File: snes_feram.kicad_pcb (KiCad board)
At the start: 2 copper layers, 98.5 x 79.5 mm, 35 parts, among them CON1 SNES-EDGE, J1 Conn_01x23_Male, J2 Conn_01x23_Male, SW1 SW_DIP_x04, U1 4081, U2 4071, U3 27C322, U5 74LS245, U6 74LS245, U7 74LS139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

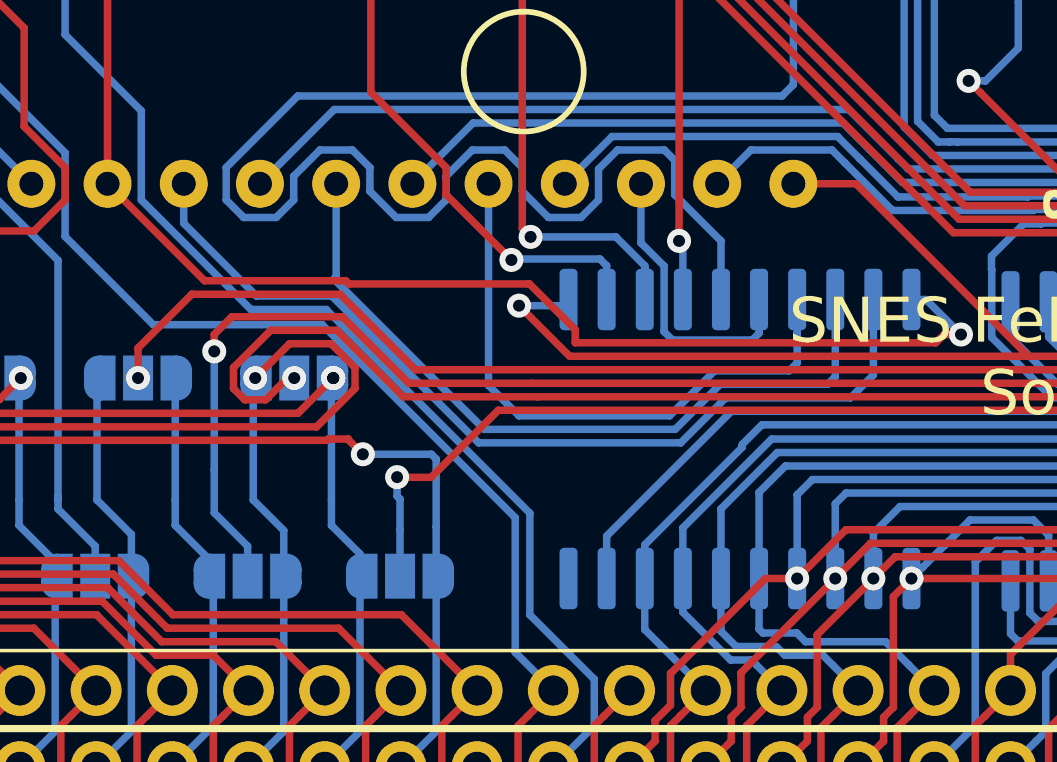
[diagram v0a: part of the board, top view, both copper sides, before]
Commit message: Corrected missing trace at pin 20 of U5, thanks to @DeLFuS
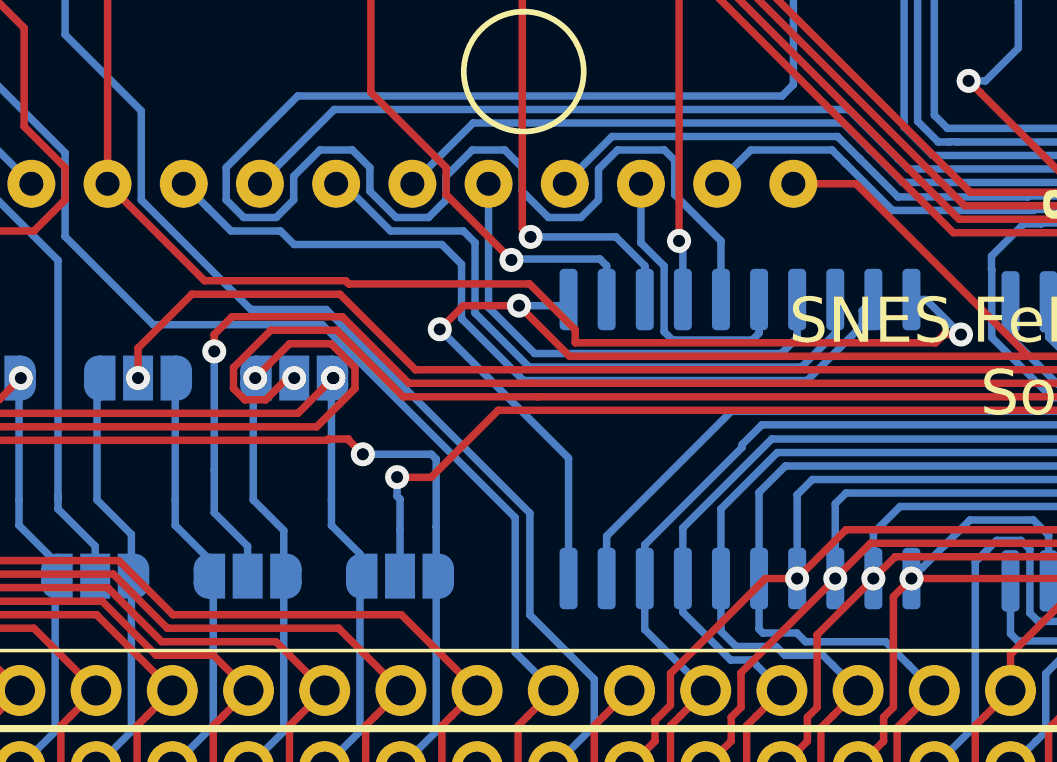
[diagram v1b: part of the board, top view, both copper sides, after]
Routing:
- net +5V: track 262.5 -> 275.5 mm, vias 10 -> 11
- net /D13: track 20.3 -> 16.5 mm
- net /D14: track 25.3 -> 22.1 mm
- net /D15: track 30.8 -> 28.2 mm
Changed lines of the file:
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@@
     (thickness 1.6)
     (drawings 48)
-    (tracks 2026)
+    (tracks 2032)
     (zones 0)
     (modules 35)
@@
       (drillshape 0)
       (scaleselection 1)
-      (outputdirectory ""))
+      (outputdirectory "Gerber/"))
   )
   (net 0 "")
@@
   (segment (start 143.41895 82.07795) (end 158.71405 82.07795) (width 0.25) (layer F.Cu) (net 2))
   (segment (start 158.71405 82.07795) (end 167.35005 82.07795) (width 0.25) (layer F.Cu) (net 2))
+  (via (at 139.0904 81.1784) (size 0.8) (drill 0.4) (layers F.Cu B.Cu) (net 2))
+  (segment (start 143.383 89.486) (end 143.383 85.471) (width 0.25) (layer B.Cu) (net 2))
+  (segment (start 143.383 85.471) (end 139.0904 81.1784) (width 0.25) (layer B.Cu) (net 2))
+  (segment (start 139.8778 80.391) (end 141.732 80.391) (width 0.25) (layer F.Cu) (net 2))
+  (segment (start 139.0904 81.1784) (end 139.8778 80.391) (width 0.25) (layer F.Cu) (net 2))
   (via (at 105.791 51.971129) (size 0.8) (drill 0.4) (layers F.Cu B.Cu) (net 3))
   (segment (start 105.791 51.405444) (end 105.791 45.388) (width 0.25) (layer F.Cu) (net 3) (status 20))
@@
   (segment (start 143.256 76.327) (end 144.831011 74.751989) (width 0.25) (layer B.Cu) (net 73))
   (segment (start 154.3644 76.76599) (end 153.099205 75.500795) (width 0.25) (layer B.Cu) (net 73))
-  (segment (start 151.003 80.186) (end 151.003 81.311) (width 0.25) (layer B.Cu) (net 74))
-  (segment (start 151.003 81.311) (end 151.003 82.296) (width 0.25) (layer B.Cu) (net 74))
-  (segment (start 150.73597 82.56303) (end 148.250855 82.563031) (width 0.25) (layer B.Cu) (net 74))
-  (segment (start 151.003 82.296) (end 150.73597 82.56303) (width 0.25) (layer B.Cu) (net 74))
-  (segment (start 148.250855 82.563031) (end 146.750906 84.06298) (width 0.25) (layer B.Cu) (net 74))
-  (segment (start 140.716 76.327) (end 140.716 83.04698) (width 0.25) (layer B.Cu) (net 74))
-  (segment (start 141.732 84.06298) (end 146.750906 84.06298) (width 0.25) (layer B.Cu) (net 74))
-  (segment (start 140.716 83.04698) (end 141.732 84.06298) (width 0.25) (layer B.Cu) (net 74))
+  (segment (start 151.003 81.4578) (end 151.003 80.186) (width 0.25) (layer B.Cu) (net 74))
+  (segment (start 150.47478 81.98602) (end 151.003 81.4578) (width 0.25) (layer B.Cu) (net 74))
+  (segment (start 142.254018 81.98602) (end 150.47478 81.98602) (width 0.25) (layer B.Cu) (net 74))
+  (segment (start 140.716 80.448002) (end 142.254018 81.98602) (width 0.25) (layer B.Cu) (net 74))
+  (segment (start 140.716 76.327) (end 140.716 80.448002) (width 0.25) (layer B.Cu) (net 74))
   (segment (start 154.518789 76.283969) (end 153.429215 75.194395) (width 0.25) (layer B.Cu) (net 75))
   (segment (start 169.010791 76.283969) (end 154.518789 76.283969) (width 0.25) (layer B.Cu) (net 75))
@@
   (segment (start 140.201021 74.301979) (end 152.536799 74.301979) (width 0.25) (layer B.Cu) (net 75))
   (segment (start 138.176 76.327) (end 140.201021 74.301979) (width 0.25) (layer B.Cu) (net 75))
-  (segment (start 152.273 80.186) (end 152.273 82.759039) (width 0.25) (layer B.Cu) (net 76))
-  (segment (start 152.018999 83.01304) (end 148.437256 83.01304) (width 0.25) (layer B.Cu) (net 76))
-  (segment (start 152.273 82.759039) (end 152.018999 83.01304) (width 0.25) (layer B.Cu) (net 76))
-  (segment (start 148.437256 83.01304) (end 146.937306 84.51299) (width 0.25) (layer B.Cu) (net 76))
-  (segment (start 140.570558 84.51299) (end 135.559568 79.502) (width 0.25) (layer B.Cu) (net 76))
-  (segment (start 146.937306 84.51299) (end 140.570558 84.51299) (width 0.25) (layer B.Cu) (net 76))
-  (segment (start 135.636 79.425568) (end 135.636 76.327) (width 0.25) (layer B.Cu) (net 76))
-  (segment (start 135.559568 79.502) (end 135.636 79.425568) (width 0.25) (layer B.Cu) (net 76))
+  (segment (start 135.874588 76.327) (end 137.449599 77.902011) (width 0.25) (layer B.Cu) (net 76))
+  (segment (start 135.636 76.327) (end 135.874588 76.327) (width 0.25) (layer B.Cu) (net 76))
+  (segment (start 139.878011 77.902011) (end 140.26599 78.28999) (width 0.25) (layer B.Cu) (net 76))
+  (segment (start 137.449599 77.902011) (end 139.878011 77.902011) (width 0.25) (layer B.Cu) (net 76))
+  (segment (start 140.265991 80.634403) (end 142.067618 82.43603) (width 0.25) (layer B.Cu) (net 76))
+  (segment (start 140.26599 78.28999) (end 140.265991 80.634403) (width 0.25) (layer B.Cu) (net 76))
+  (segment (start 152.273 81.311) (end 152.273 80.186) (width 0.25) (layer B.Cu) (net 76))
+  (segment (start 151.14797 82.43603) (end 152.273 81.311) (width 0.25) (layer B.Cu) (net 76))
+  (segment (start 142.067618 82.43603) (end 151.14797 82.43603) (width 0.25) (layer B.Cu) (net 76))
   (segment (start 169.197191 75.833959) (end 154.705189 75.833959) (width 0.25) (layer B.Cu) (net 77))
   (segment (start 171.520037 78.156805) (end 169.197191 75.833959) (width 0.25) (layer B.Cu) (net 77))
@@
   (segment (start 133.096 76.327) (end 135.571031 73.851969) (width 0.25) (layer B.Cu) (net 77))
   (segment (start 154.705189 75.833959) (end 154.370615 75.499385) (width 0.25) (layer B.Cu) (net 77))
-  (segment (start 153.543 80.186) (end 153.543 82.701048) (width 0.25) (layer B.Cu) (net 78))
-  (segment (start 152.781 83.463048) (end 148.623657 83.463049) (width 0.25) (layer B.Cu) (net 78))
-  (segment (start 153.543 82.701048) (end 152.781 83.463048) (width 0.25) (layer B.Cu) (net 78))
-  (segment (start 147.123706 84.963) (end 140.384158 84.963) (width 0.25) (layer B.Cu) (net 78))
-  (segment (start 148.623657 83.463049) (end 147.123706 84.963) (width 0.25) (layer B.Cu) (net 78))
-  (segment (start 140.384158 84.963) (end 135.489148 80.06799) (width 0.25) (layer B.Cu) (net 78))
-  (segment (start 135.489148 80.06799) (end 132.9784 80.06799) (width 0.25) (layer B.Cu) (net 78))
-  (segment (start 130.556 77.64559) (end 130.556 76.327) (width 0.25) (layer B.Cu) (net 78))
-  (segment (start 132.9784 80.06799) (end 130.556 77.64559) (width 0.25) (layer B.Cu) (net 78))
+  (segment (start 131.355999 77.126999) (end 130.556 76.327) (width 0.25) (layer B.Cu) (net 78))
+  (segment (start 132.131011 77.902011) (end 131.355999 77.126999) (width 0.25) (layer B.Cu) (net 78))
+  (segment (start 133.782011 77.902011) (end 132.131011 77.902011) (width 0.25) (layer B.Cu) (net 78))
+  (segment (start 134.232021 78.352021) (end 133.782011 77.902011) (width 0.25) (layer B.Cu) (net 78))
+  (segment (start 139.159621 78.352021) (end 134.232021 78.352021) (width 0.25) (layer B.Cu) (net 78))
+  (segment (start 153.17229 80.55671) (end 153.17229 81.04812) (width 0.25) (layer B.Cu) (net 78))
+  (segment (start 153.17229 81.04812) (end 151.334371 82.886039) (width 0.25) (layer B.Cu) (net 78))
+  (segment (start 153.543 80.186) (end 153.17229 80.55671) (width 0.25) (layer B.Cu) (net 78))
+  (segment (start 151.334371 82.886039) (end 141.881217 82.886039) (width 0.25) (layer B.Cu) (net 78))
+  (segment (start 141.881217 82.886039) (end 139.815982 80.820802) (width 0.25) (layer B.Cu) (net 78))
+  (segment (start 139.815982 79.008382) (end 139.159621 78.352021) (width 0.25) (layer B.Cu) (net 78))
+  (segment (start 139.815982 80.820802) (end 139.815982 79.008382) (width 0.25) (layer B.Cu) (net 78))
   (via (at 165.735 78.486) (size 0.8) (drill 0.4) (layers F.Cu B.Cu) (net 79))
   (segment (start 167.005 79.756) (end 165.735 78.486) (width 0.25) (layer B.Cu) (net 79))

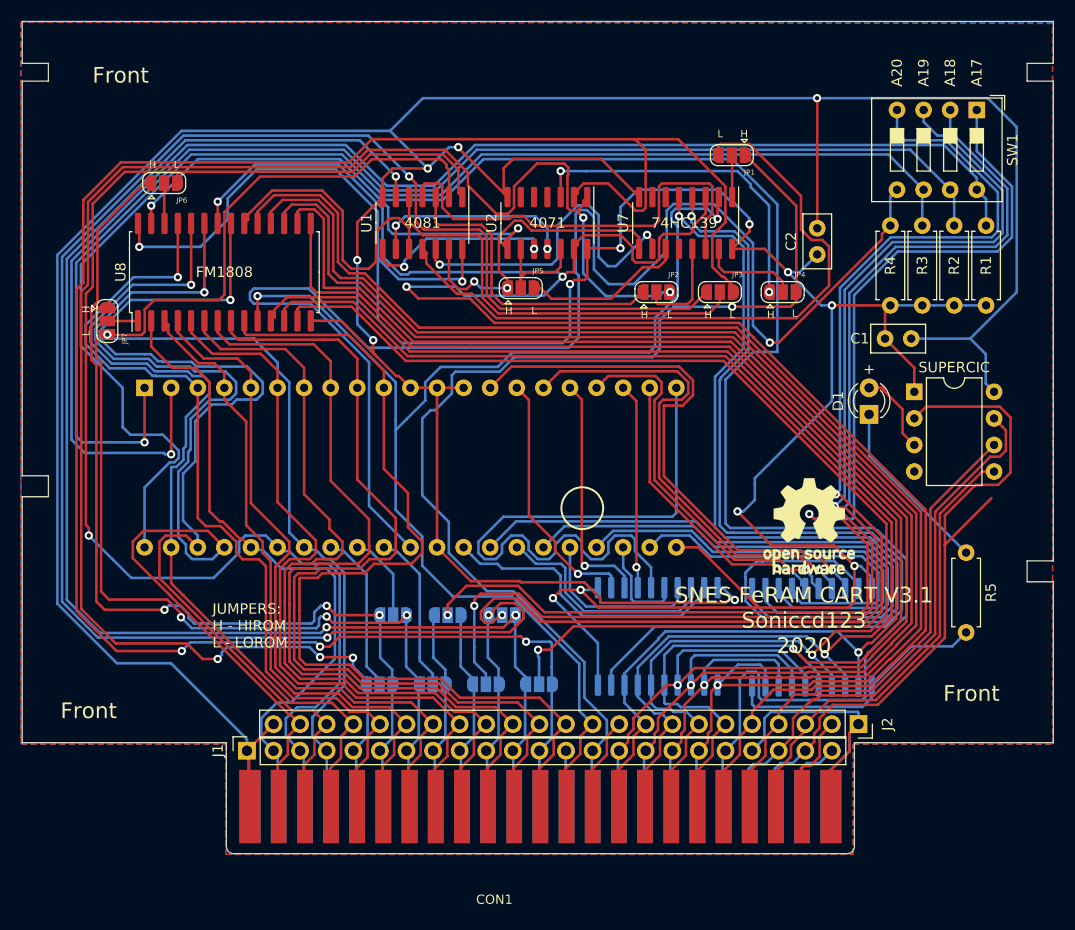
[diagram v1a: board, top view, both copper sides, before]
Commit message: -Upgrade to kicad6 -Fixed ERC errors -Edited soic footprints to indicate pin1 with a circle -Added Slash to Low asserted signals -Fixed byte swapping
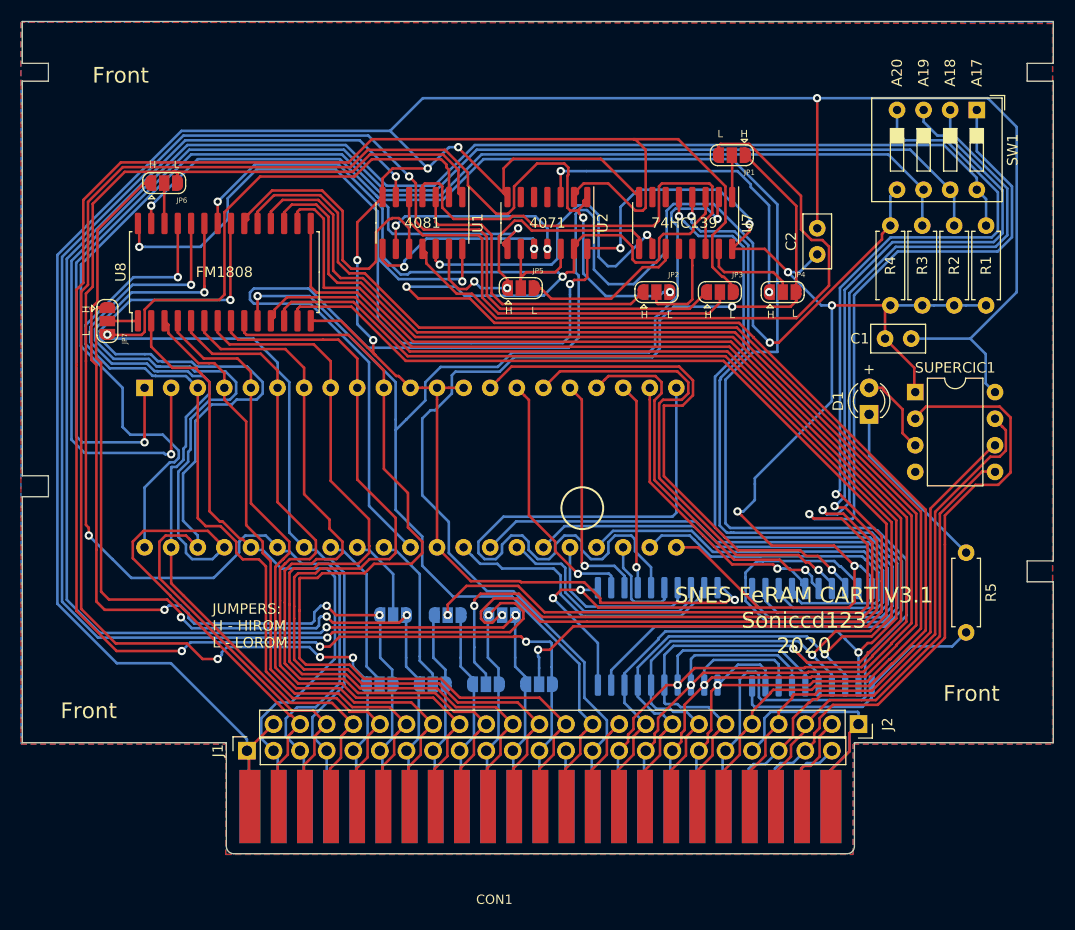
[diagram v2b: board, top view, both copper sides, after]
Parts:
- removed G***: LOGO, OPEN:open_hardware
- removed SUPERCIC: PIC12F629-IMC, Package_DIP:DIP-8_W7.62mm
- added SUPERCIC1: PIC12F629-IMC, Package_DIP:DIP-8_W7.62mm, F.Cu at (173.7, 61.5)
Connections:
- J1 pad 14: /CART -> //CART
- J1 pad 19: /WR -> //WR
- J2 pad 10: /IRQ -> //IRQ
- J2 pad 2: /RESET -> //RESET
- J2 pad 5: /RD -> //RD
- JP1 pad 1: /CART -> //CART
- JP4 pad 3: /CART -> //CART
- U2 pad 13: /RD -> //RD
- U2 pad 8: /WR -> //WR
- U7 pad 12: (no net) -> unconnected-(U7-Pad12)
- U7 pad 3: /RD -> //RD
- U7 pad 4: /BYTE_1 -> /BYTE_0
- U7 pad 5: /BYTE_0 -> /BYTE_1
- U7 pad 6: (no net) -> unconnected-(U7-Pad6)
- U7 pad 7: (no net) -> unconnected-(U7-Pad7)
- U8 pad 22: /RD -> //RD
- U8 pad 27: /WR -> //WR
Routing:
- net /RD: track 183.6 -> 0.00 mm, vias 3 -> 0
- net //WR: track 0.00 -> 182.7 mm, vias 0 -> 2
- net /WR: track 182.7 -> 0.00 mm, vias 2 -> 0
- net //RD: track 0.00 -> 180.1 mm, vias 0 -> 3
- net //CART: track 0.00 -> 105.6 mm, vias 0 -> 1
- net /CART: track 105.6 -> 0.00 mm, vias 1 -> 0
- net /IRQ: track 9.09 -> 0.00 mm
- net /CIC_CLK: track 67.1 -> 60.8 mm
- net //IRQ: track 0.00 -> 5.44 mm
- net /CIC_OUT: track 48.6 -> 45.1 mm
- net /BYTE_1: track 91.7 -> 90.5 mm
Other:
- net class Default removed

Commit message: -Fixed footprint library missing -Updated soic footprints -Updated version number
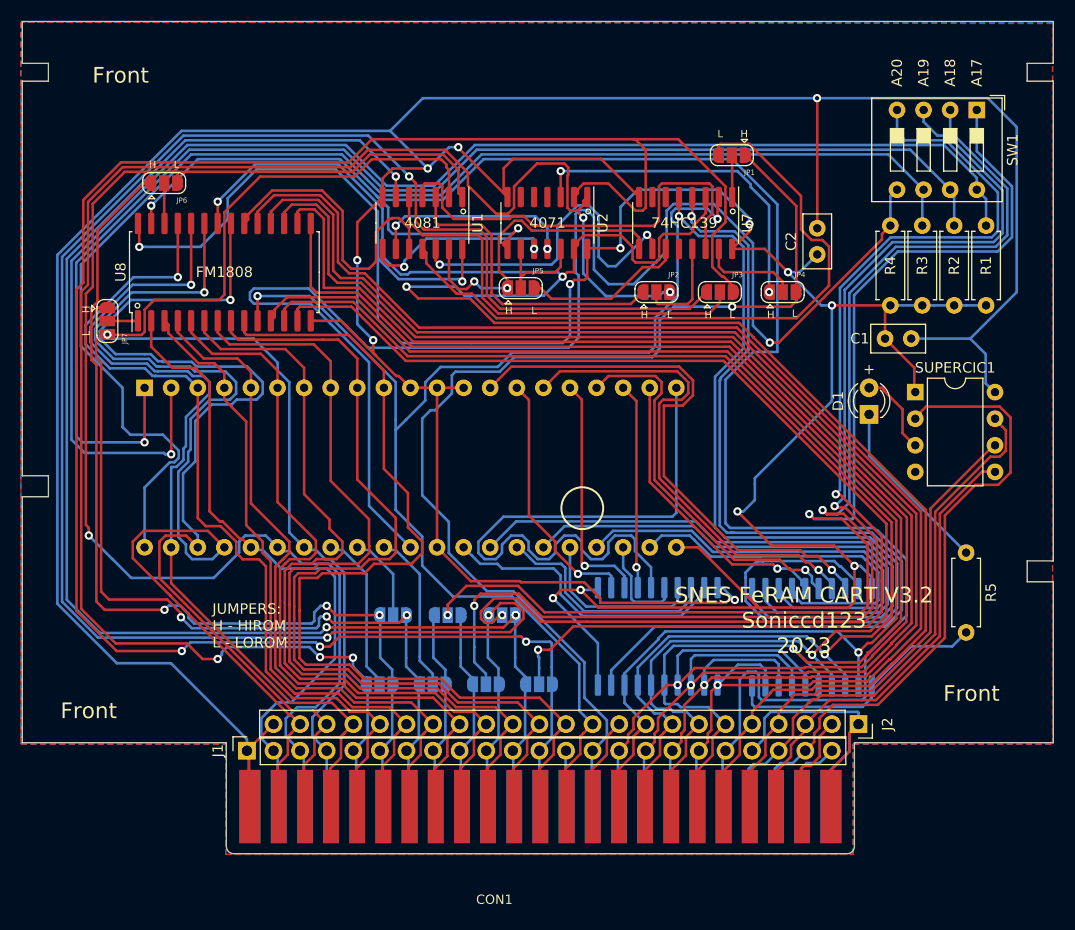
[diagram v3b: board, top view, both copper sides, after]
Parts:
- U1, U2: footprint Package_SO:SOIC-14_3.9x8.7mm_P1.27mm -> footprints:SOIC-14_3.9x8.7mm_P1.27mm
- U5, U6: footprint Package_SO:SOIC-20W_7.5x12.8mm_P1.27mm -> footprints:SOIC-20W_7.5x12.8mm_P1.27mm
- U7: footprint Package_SO:SOIC-16_3.9x9.9mm_P1.27mm -> footprints:SOIC-16_3.9x9.9mm_P1.27mm
- U8: footprint Package_SO:SOIC-28W_7.5x17.9mm_P1.27mm -> footprints:SOIC-28W_7.5x17.9mm_P1.27mm
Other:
- board text added: "SNES FeRAM CART V3.2 Soniccd123 2023"
- board text removed: "SNES FeRAM CART V3.1 Soniccd123 2020"
